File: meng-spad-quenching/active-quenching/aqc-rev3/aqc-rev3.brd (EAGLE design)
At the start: 120 x 74.9 mm, 252 parts, among them IC1 TPS7A4901, IC10 TPS7A3001, IC11 LT1534-1, IC12 74AHC1G04DBV, IC13 TLV271DBV, IC14 NC7WZ16P6X, IC15 LTC1711, IC16 HFA3134, IC17 HFA3135, IC18 USBLC6-2SC6Y, IC19 HFA3135, IC2 TPS7A4901, IC20 HFA3134, IC21 STM32F411RE, IC22 MAX572X, IC23 HFA3134, IC24 LM1117, IC25 HFA3134, IC26 THAT320, IC3 LT1534-1, IC4 TLV272DGK, IC5 ADCMP582, IC6 DS1100LU-20+, IC7 HFA3134, IC8 NC7SV74K8X, IC9 HFA3134, M1 BSS806N, M2 BSS806N, M3 BSS806N, Q6 IRLML6402TRPBF, SW1 MCU_RST, U1 MCP4725, U2 SN65EPT22DGK, U3 SN65EPT21DGK, X1 CONN_PULLDN_SENSE, X2 CONN_FORCE_QUENCH, X3 KEYSTONE-7774, X4 CONN_SPAD, X5 CONN_PHOTON_COUNTER, X6 KEYSTONE-7774, X7 CONN_SMU, X8 PN61729-S

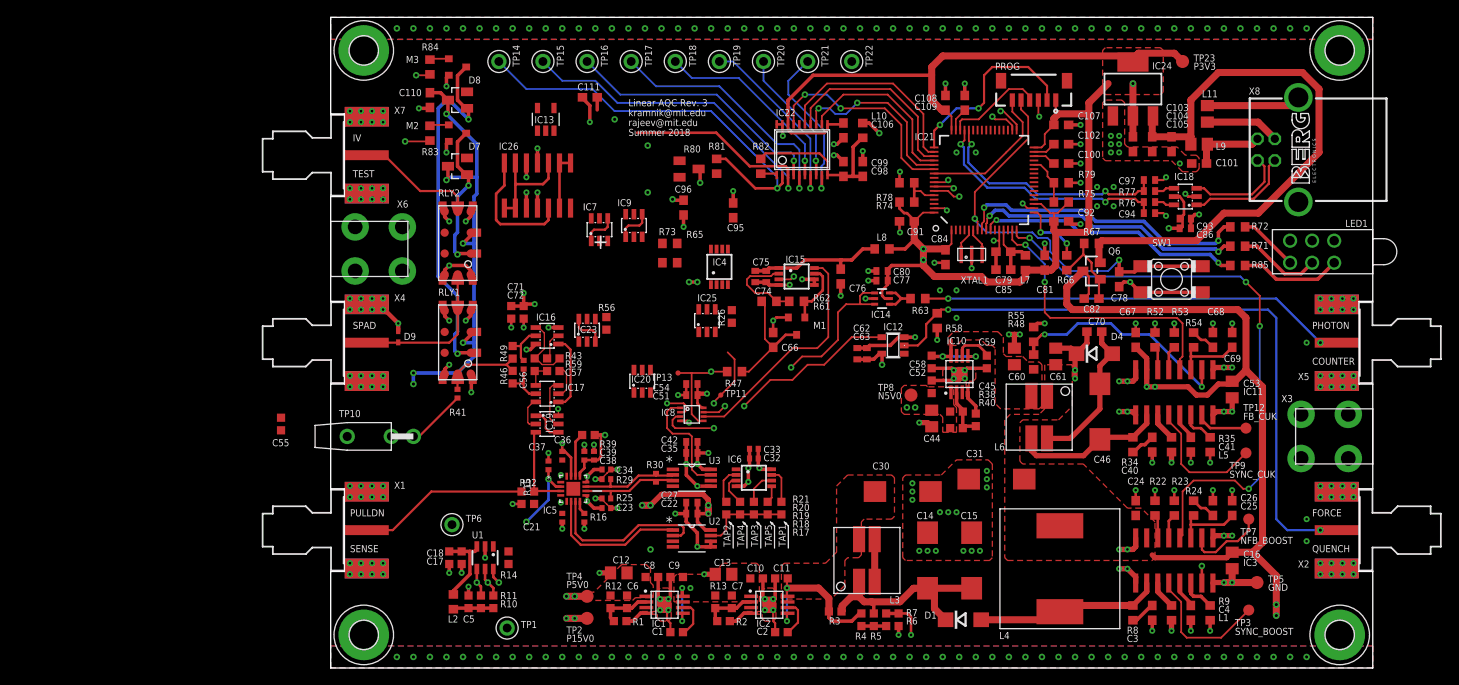
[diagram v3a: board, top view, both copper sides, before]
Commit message: Improvements to one-shot and logic, more layout
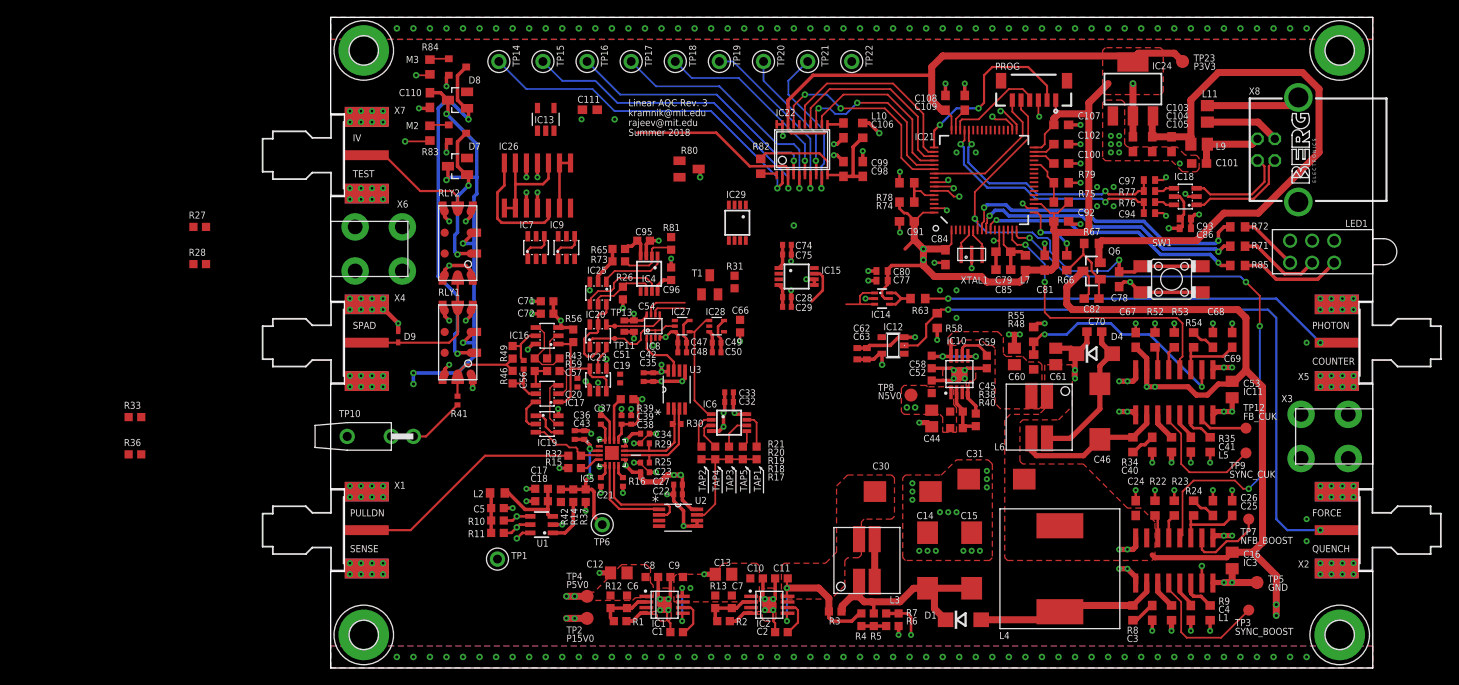
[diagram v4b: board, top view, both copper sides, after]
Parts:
- removed C55: 100n, rcl-modified-footprints:C0603
- removed C76: 4u7, rcl:C0603
- removed L8: PE-0603FB601ST, meng:R0603
- removed M1: BSS806N, meng:SOT23R_INFINEON
- removed R47, R61: 1k, rcl:R0603
- removed R62: 10k, rcl:R0603
- added C19, C20, C28, C47, C49: 10n, rcl-modified-footprints:C0402
- added C29, C43, C48, C50: 100n, rcl-modified-footprints:C0402
- added IC27: 74AHC1G14DCK, 74xx-little-de:SC70-5
- added IC28: NL17SZ125, 74xx-little-de:SC70-5
- added IC29: TLV272DGK, meng:MSOP8
- added R27, R28: 220k, rcl-modified-footprints:R0603
- added R31: 10k, rcl-modified-footprints:R0603
- added R33, R36: 100k, rcl-modified-footprints:R0603
- added R37, R42: DNP, rcl-modified-footprints:R0603
- added T1: MMBTH10, transistor:SOT23-BEC
- C21: value 10n -> 100n
- C22, C27, C35, C42, C74, C75: device rcl:C0402 -> rcl-modified-footprints:C0402
- C36: value 1n -> 10n
- C37: value 100n -> 10n
- C66: value 470p -> 100p; device rcl:C0603 -> rcl-modified-footprints:C0603
- C95, C96: device rcl:C0603 -> rcl-modified-footprints:C0603
- R14: value 100R -> 1k
- R65: device rcl:R0603 -> rcl-modified-footprints:R0603
- R73, R81: value 100k -> 220k; device rcl:R0603 -> rcl-modified-footprints:R0603
- TP14: value CASC_IBIAS -> DELTA_V
- TP17: value SLEW_UP -> V_A
- TP18: value SLEW_DN -> EXTRA_1
- TP19: value SLEW_MAX -> EXTRA_2
- TP20: value (DELAY_UP) -> EXTRA_3
- TP21: value (DELAY_DN) -> EXTRA_4
- moved TP6 17.3 mm to (31.3, 16.5)
- moved TP11 13.8 mm to (32.7, 37.9)
- moved L2 13.5 mm to (19.2, 20.2), turned to 0 degrees
- moved C17 13.3 mm to (24.3, 20.6), turned to 180 degrees
- moved IC25 12.9 mm to (30.8, 43.2), turned to 180 degrees
- moved R26 12.8 mm to (33.7, 43.2)
- moved C5 11.3 mm to (19.2, 18.4), turned to 0 degrees
- moved C18 11.3 mm to (24.3, 19.2), turned to 180 degrees
- moved IC8 11.1 mm to (37.1, 39.4), turned to 0 degrees
- moved C95 10.9 mm to (36.0, 49.2), turned to 0 degrees
- moved C51 10.4 mm to (34.9, 39.4), turned to 270 degrees
- moved R14 10.3 mm to (27.9, 19.8)
- moved R81 10.3 mm to (39.2, 48.9)
- moved U3 10.3 mm to (39.8, 32.1), turned to 90 degrees
- moved C54 10.2 mm to (33.8, 39.4), turned to 270 degrees
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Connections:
- net N$28 renamed PULLDN_SENSE_R_CONN
- removed net COMP_VP: C36.1, IC5.2, R14.1
- removed net N$25: IC15.2, R61.1, R62.2
- removed net PP_P3V3_COMP: C74.1, C75.1, C76.1, IC15.1, L8.2
- removed net PP_P3V3_DAC2: C17.1, C18.1, L2.2, U1.3
- removed net VREF_EXTRA_1: IC22.6, TP18.P$1
- removed net VREF_ONE_SHOT: IC15.3, IC22.4, TP16.P$1
- new net LOGIC_QUENCH_BUF: IC14.1, IC14.3, IC27.4, IC28.1, IC6.1
- new net N$1: R14.2, U1.1
- new net N$10: IC29.6, R33.2, R36.1
- new net N$5: IC29.1, T1.B
- new net N$7: IC15.3, IC29.7, R33.1
- new net ONE_SHOT_FB: R27.1, R31.1, T1.E
- new net ONE_SHOT_VGND: IC29.2, R27.2, R28.1
- new net PP_P3V3_AV_DET_DAC: C17.1, C18.1, L2.2, R42.2, U1.3
- new net VREF_ONE_SHOT_CCS: IC22.6, R28.2, TP18.P$1
- new net VREF_ONE_SHOT_COMP: IC22.4, IC29.5, TP16.P$1
- net !LOGIC_QUENCH: now also IC27.2
- net GND: now also C19.2, C20.2, C28.2, C29.2, C43.2, C47.2, C48.2, C49.2, C50.2, IC27.3, IC28.3, IC29.3, R37.1; no longer C55.2, C76.2, IC15.4, M1.2
- net LOGIC_QUENCH: no longer IC14.1, IC14.3, IC6.1, R47.2
- net ONE_SHOT_CAP: now also IC15.2, IC28.4, T1.C; no longer M1.3, R47.1, R61.2
- net ONE_SHOT_CLR: no longer M1.1, R62.1
- net PP_N5V0_ANALOG: now also C28.1, C29.1, IC15.4, IC29.4, R31.2
- net PP_P15V0_ANALOG: no longer C55.1
- net PP_P3V3: now also C47.1, C48.1, C49.1, C50.1, IC27.5, IC28.2, IC28.5; no longer L8.1
- net PP_P5V0_ANALOG: now also C19.1, C20.1, C74.1, C75.1, IC15.1, IC29.8, R36.2
- net VREF_AV_DET: now also C36.1, C43.1, IC5.2, R14.1, R37.2, R42.1; no longer R14.2, U1.1
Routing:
- net VREF_ONE_SHOT: track 45.8 -> 0.00 mm, vias 2 -> 0
- net PP_P5V0_ANALOG: track 112.8 -> 72.9 mm, vias 9 -> 8
- net VREF_ONE_SHOT_COMP: track 0.00 -> 38.0 mm, vias 0 -> 2
- net PP_N5V0_ANALOG: track 88.8 -> 51.3 mm, vias 5 -> 3
- net LOGIC_QUENCH: track 38.9 -> 7.14 mm, vias 2 -> 0
- net PP_P3V3: track 279.1 -> 252.7 mm, vias 17 -> 14
- net !ONE_SHOT_CLR: track 27.3 -> 3.98 mm
- net VREF_ONE_SHOT_CCS: track 0.00 -> 22.4 mm, vias 0 -> 1
- net VREF_EXTRA_1: track 22.4 -> 0.00 mm, vias 1 -> 0
- net DAC2_ADDRSEL: track 161.8 -> 141.8 mm
- net LOGIC_QUENCH_BUF: track 0.00 -> 19.4 mm
- net !FORCE_QUENCH: track 24.1 -> 4.92 mm, vias 2 -> 0
- net DAC2_SCL: track 161.0 -> 142.3 mm
- net DAC2_SDA: track 159.4 -> 141.8 mm
- net VREF_AV_DET: track 0.00 -> 16.6 mm, vias 0 -> 2
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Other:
- board text removed: "+"

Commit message: work on layout
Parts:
- added C55, C76: 10n, rcl:C0402
- added C64, C65, C73, C83: 100n, rcl:C0402
- added IC30: 74AHC1G32DCK, 74xx-little-de:SC70-5
- added IC31: 74AHC1G08DCK, 74xx-little-de:SC70-5
- added R44: 49R9, rcl:R0603
- IC12: value 74AHC1G04DBV -> 74AHC1G04DCK; device 74xx-little-de:SOT23-5 -> 74xx-little-de:SC70-5
- moved IC9 21.5 mm to (20.2, 28.1), turned to 90 degrees
- moved R80 13.4 mm to (28.3, 54.1)
- moved IC13 11.9 mm to (32.5, 54.1), turned to 180 degrees
- moved C111 11.6 mm to (35.4, 54.1), turned to 90 degrees
- moved IC26 8.94 mm to (24.8, 46.7), turned to 270 degrees
- moved R31 8.40 mm to (44.3, 52.5)
- moved IC7 5.71 mm to (23.7, 54.1), turned to 270 degrees
- moved IC12 5.26 mm to (60.2, 39.7)
- moved T1 4.39 mm to (47.9, 43.2), turned to 180 degrees
- moved C71 2.78 mm to (27.3, 40.8), turned to 0 degrees
- moved R65 2.43 mm to (30.8, 47.8)
- moved R73 2.43 mm to (30.8, 46.4)
- moved C63 2.14 mm to (60.2, 37.6), turned to 0 degrees
- moved C62 0.57 mm to (60.2, 36.5), turned to 0 degrees
- moved C72 0.48 mm to (24.4, 40.8)
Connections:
- net ONE_SHOT_CLR renamed NC_ONE_SHOT_CLR
- removed net DAC1_CSB: IC21.50, IC22.15
- new net DFLOP_!CLR: IC31.4, IC8.6
- new net FORCE_QUENCH_USER: IC30.1, R58.2, X2.1
- new net MCU_TIM2_CH1_IN: IC21.14, R44.1
- new net MCU_TIM2_CH1_OUT_1: IC21.21, IC31.1
- new net MCU_TIM2_CH1_OUT_2: IC21.50, IC30.2
- net !ONE_SHOT_CLR: now also IC31.2; no longer IC8.6
- net FORCE_QUENCH: now also IC30.4; no longer R58.2, X2.1
- net GND: now also C55.2, C64.2, C65.2, C73.2, C76.2, C83.2, IC22.15, IC30.3, IC31.3
- net LOGIC_QUENCH_BUF: now also R44.2
- net PP_N5V0_ANALOG: now also C73.1
- net PP_P3V3: now also C55.1, C64.1, C76.1, C83.1, IC30.5, IC31.5
- net PP_P5V0_ANALOG: now also C65.1
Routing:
- net FORCE_QUENCH_USER: track 0.00 -> 76.5 mm, vias 0 -> 2
- net FORCE_QUENCH: track 76.5 -> 0.00 mm, vias 2 -> 0
- net N$16: track 0.00 -> 24.0 mm, vias 0 -> 1
- net MCU_TIM2_CH1_OUT_2: track 0.00 -> 23.9 mm, vias 0 -> 2
- net DAC1_CSB: track 23.9 -> 0.00 mm
- net DIAMOND_IBIAS_MID: track 6.47 -> 27.6 mm, vias 0 -> 2
- net N$26: track 0.00 -> 18.6 mm, vias 0 -> 1
- net PP_P3V3: track 252.7 -> 266.4 mm
- net DIAMOND_BASE: track 4.13 -> 15.0 mm
- net DIAMOND_IBIAS_BOTTOM: track 3.14 -> 10.4 mm, vias 0 -> 2
- net DIAMOND_FB: track 0.18 -> 6.72 mm
- net MCU_JTCK: track 22.4 -> 27.7 mm
- net DIAMOND_IBIAS_TOP: track 8.07 -> 12.6 mm
- net NC_ONE_SHOT_CLR: track 4.48 -> 0.00 mm
- net !ONE_SHOT_CLR: track 3.98 -> 0.00 mm
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
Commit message: work on layout
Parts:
- removed C102: 100n, rcl:C0603
- added R45: 0R, resistor:R0603
- C76, C83: device rcl:C0402 -> rcl-modified-footprints:C0402
- R44: device rcl:R0603 -> rcl-modified-footprints:R0603
- moved C64 98.6 mm to (63.5, 36.5)
- moved C55 98.6 mm to (63.5, 37.6)
- moved C65 91.6 mm to (53.7, 51.6), turned to 180 degrees
- moved C73 91.6 mm to (53.7, 46.5)
- moved R33 84.0 mm to (58.9, 49.4), turned to 270 degrees
- moved R36 83.8 mm to (57.5, 49.4), turned to 90 degrees
- moved R27 65.0 mm to (49.8, 48.7), turned to 90 degrees
- moved R28 63.5 mm to (48.4, 48.7), turned to 90 degrees
- moved IC29 7.18 mm to (53.7, 49.1), turned to 270 degrees
- moved R31 7.13 mm to (46.8, 45.9)
- moved C74 4.84 mm to (48.9, 45.6), turned to 90 degrees
- moved C75 3.27 mm to (50.0, 45.6), turned to 90 degrees
- moved T1 1.28 mm to (47.8, 41.9)
- moved C29 1.27 mm to (52.5, 40.3)
- moved IC15 1.27 mm to (53.7, 43.8)
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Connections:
- net GND: now also R45.2; no longer C102.2
- net MCU_VCAP_1: now also R45.1; no longer C102.1
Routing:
- net PP_P3V3: track 266.4 -> 362.8 mm, vias 14 -> 20
- net PP_P5V0_ANALOG: track 72.7 -> 115.6 mm, vias 9 -> 8
- net GND: track 280.2 -> 294.8 mm, vias 361 -> 368
- net VREF_DELTAV_SETPOINT: track 40.6 -> 55.0 mm
- net N$7: track 0.00 -> 12.5 mm
- net N$16: track 24.0 -> 35.2 mm, vias 1 -> 2
- net N$26: track 18.6 -> 28.2 mm, vias 1 -> 2
- net DFLOP_!CLR: track 0.00 -> 7.45 mm
- net DIAMOND_FB: track 6.72 -> 12.0 mm
- net ONE_SHOT_CAP: track 0.00 -> 4.14 mm
- net ONE_SHOT_VGND: track 0.00 -> 3.84 mm
- net VREF_ONE_SHOT_COMP: track 38.0 -> 34.5 mm
- net N$10: track 0.00 -> 3.22 mm
- net ONE_SHOT_FB: track 0.00 -> 2.14 mm
- net FORCE_QUENCH: track 0.00 -> 1.90 mm
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
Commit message: First-pass layout complete
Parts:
- C100, C107, C91, C92: device rcl:C0603 -> rcl-modified-footprints:C0603
- C65, C73: device rcl:C0402 -> rcl-modified-footprints:C0402
- R45, R74, R75, R78, R79: device resistor:R0603 -> rcl-modified-footprints:R0603
- moved C75 4.85 mm to (52.5, 41.4), turned to 0 degrees
- moved C28 4.76 mm to (52.5, 36.7)
- moved C29 4.76 mm to (52.5, 35.6)
- moved IC15 4.76 mm to (53.7, 39.1)
- moved C74 4.74 mm to (52.5, 42.5), turned to 0 degrees
- moved R28 3.19 mm to (47.0, 45.9)
- moved R27 3.19 mm to (48.4, 45.9)
- moved C73 3.07 mm to (52.5, 43.7)
- moved R31 3.02 mm to (49.8, 45.9)
- moved C65 2.86 mm to (53.7, 48.7)
- moved IC29 2.86 mm to (53.7, 46.2)
- moved R33 2.86 mm to (58.9, 46.5)
- moved R36 2.86 mm to (57.5, 46.5)
- moved C107 1.59 mm to (84.1, 61.0)
- moved C30 1.43 mm to (65.9, 21.7)
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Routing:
- net PP_N5V0_ANALOG: track 54.6 -> 119.5 mm, vias 3 -> 7
- net PP_P5V0_ANALOG: track 115.6 -> 173.1 mm, vias 8 -> 13
- net MCU_TIM2_CH1_OUT_1: track 0.00 -> 46.7 mm, vias 0 -> 2
- net MCU_TIM2_CH1_IN: track 0.00 -> 46.1 mm, vias 0 -> 2
- net VREF_VA_SETPOINT: track 29.6 -> 62.4 mm, vias 1 -> 4
- net !FORCE_QUENCH: track 4.72 -> 26.5 mm, vias 1 -> 2
- net VREF_ONE_SHOT_COMP: track 34.5 -> 54.2 mm
- net LOGIC_QUENCH_BUF: track 19.6 -> 38.3 mm, vias 0 -> 2
- net !ONE_SHOT_CLR: track 0.00 -> 16.2 mm, vias 0 -> 2
- net VREF_ONE_SHOT_CCS: track 22.4 -> 37.3 mm
- net N$5: track 0.00 -> 7.22 mm, vias 0 -> 2
- net PP_P3V3: track 362.8 -> 367.6 mm, vias 20 -> 19
- net ONE_SHOT_CAP: track 4.14 -> 8.56 mm
- net ONE_SHOT_VGND: track 3.84 -> 6.39 mm
- net ONE_SHOT_FB: track 2.14 -> 4.45 mm
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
